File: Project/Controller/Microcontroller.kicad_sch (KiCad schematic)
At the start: 35 parts, among them J2 SWD Connector, J3 USB_B_Micro, SW1 SW_SPDT, SW2 SW_SPDT, SW3 SW_Push, U1 STM32F446RCTx, U2 TVS0500DRV, Y1 25 MHz

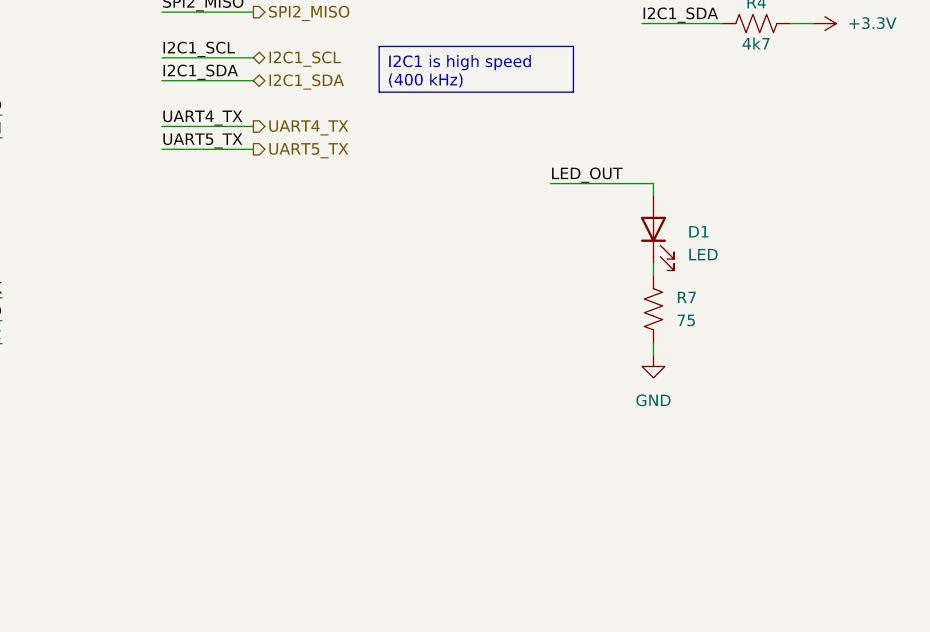
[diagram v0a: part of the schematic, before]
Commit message: Add 64 kb EEPROM
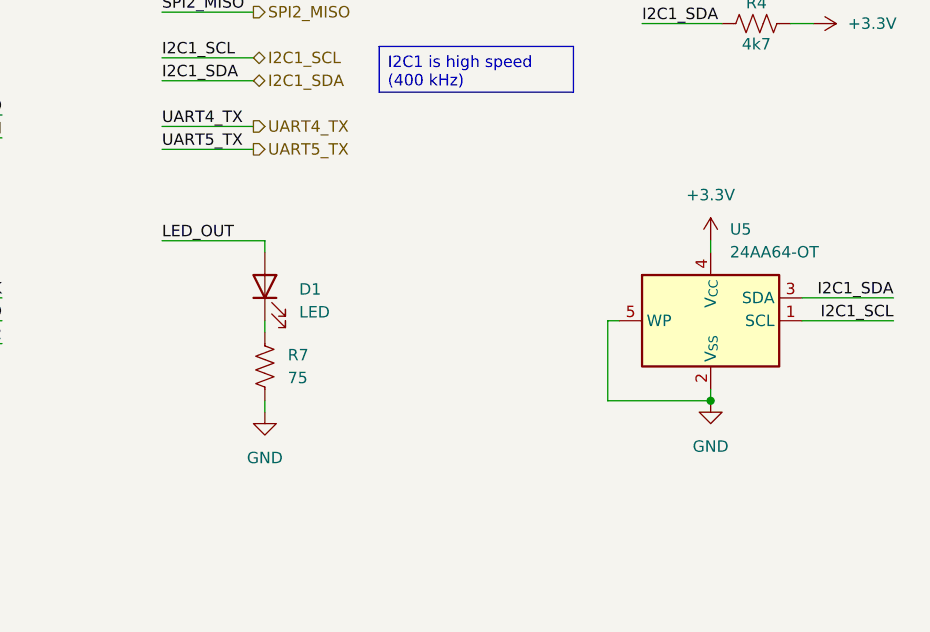
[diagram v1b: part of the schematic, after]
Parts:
- added U5: 24AA64-OT, Package_TO_SOT_SMD:SOT-23-5, symbol Memory_EEPROM:24AA02-OT
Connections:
- net +3.3V: now also U5.4 (V_{CC})
- net GND: now also U5.2 (V_{SS}), U5.5 (WP)
- net I2C1_SCL: now also U5.1 (SCL)
- net I2C1_SDA: now also U5.3 (SDA)
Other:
- moved on the sheet: D1, R7

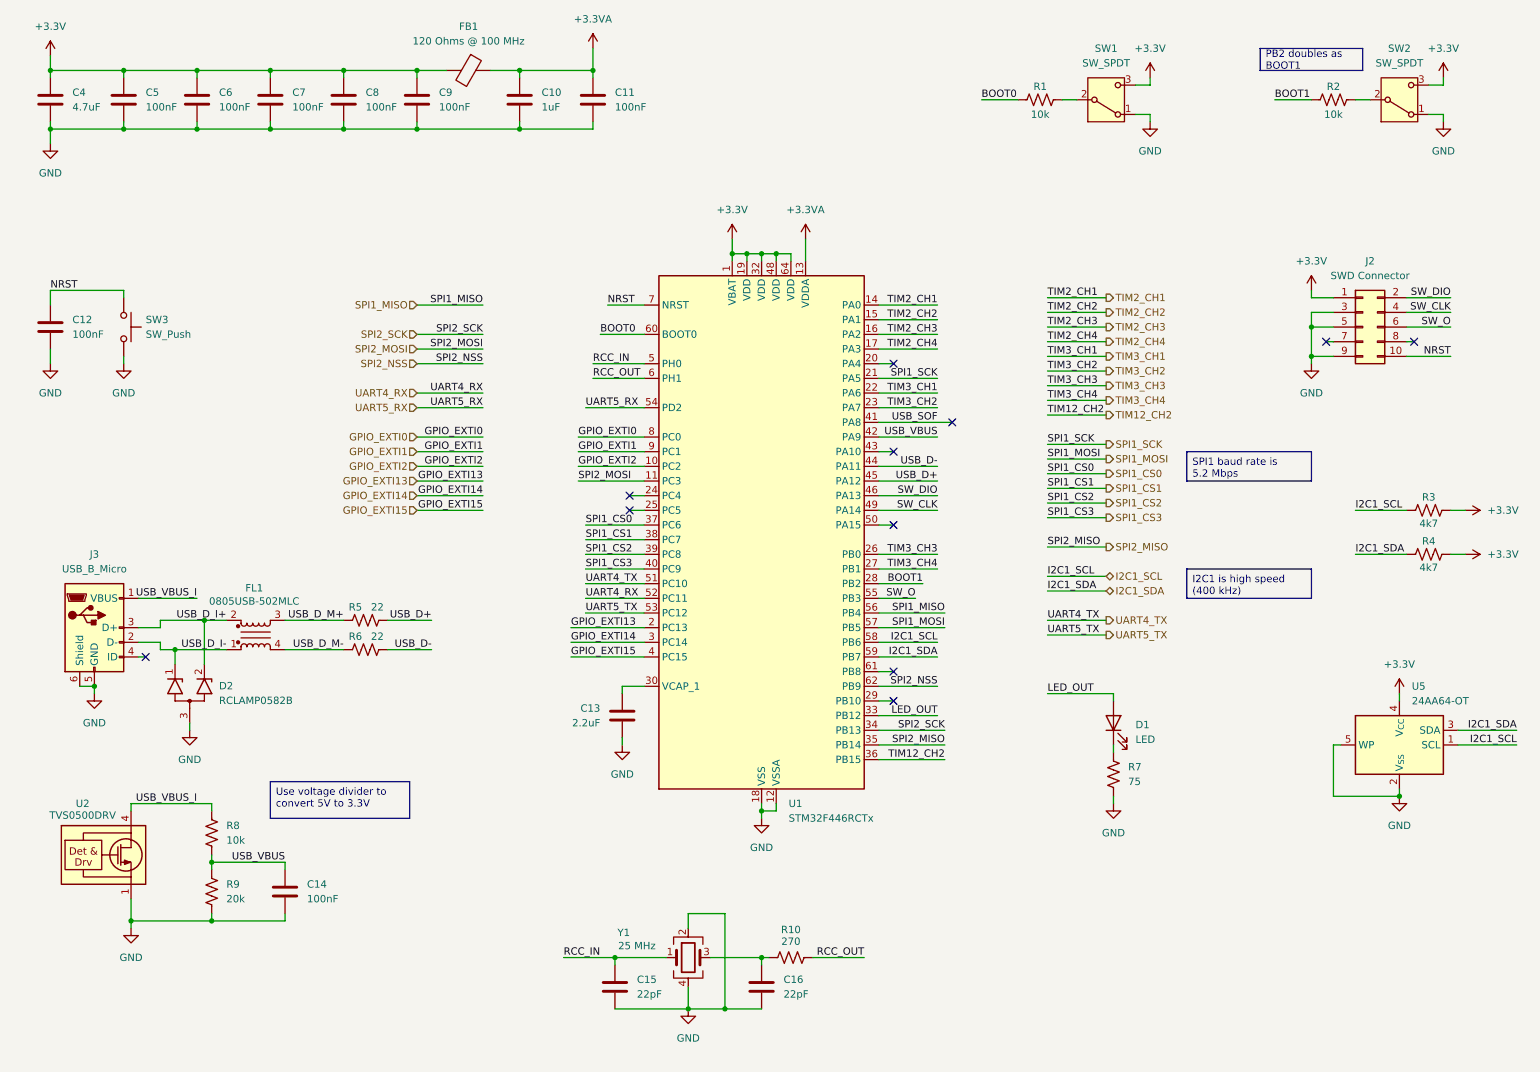
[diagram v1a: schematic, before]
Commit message: Add LDO to power input for controller board
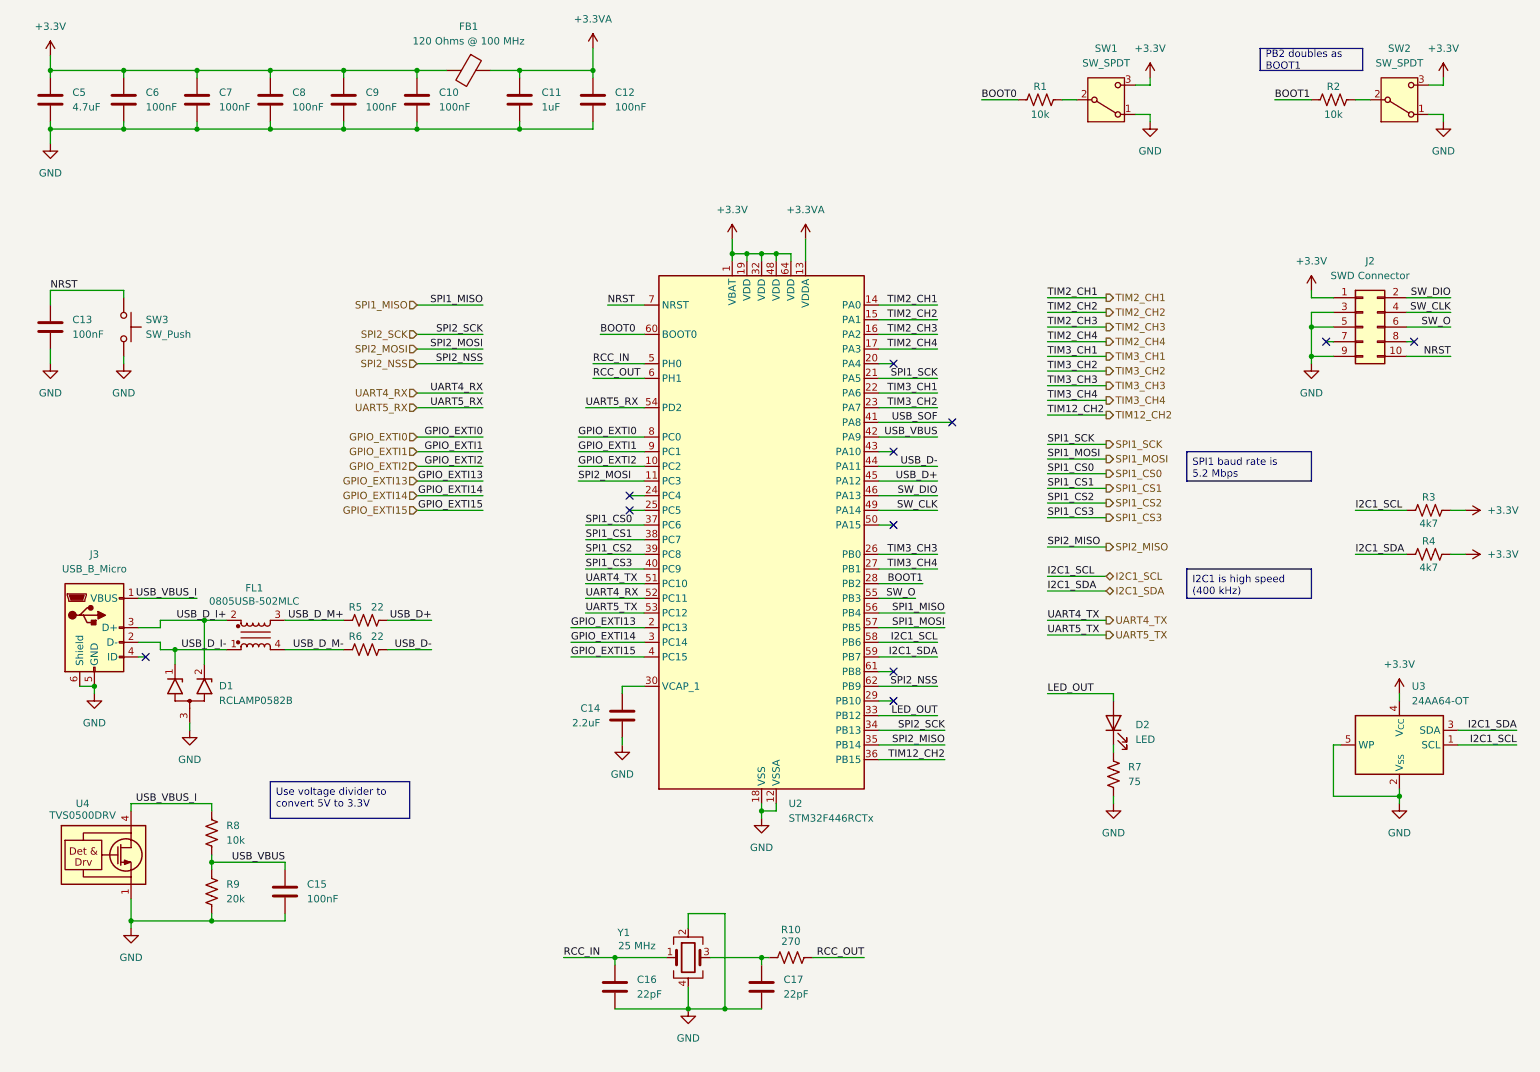
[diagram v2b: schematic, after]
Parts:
- renumbered C9 to C10, C10 to C11, C11 to C12, C12 to C13, C13 to C14, C14 to C15, C15 to C16, C16 to C17, C4 to C5, C5 to C6, C6 to C7, C7 to C8, C8 to C9, D2 to D1, D1 to D2, U1 to U2, U5 to U3, U2 to U4

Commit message: Change USB connector from USB-B Micro to USB-C
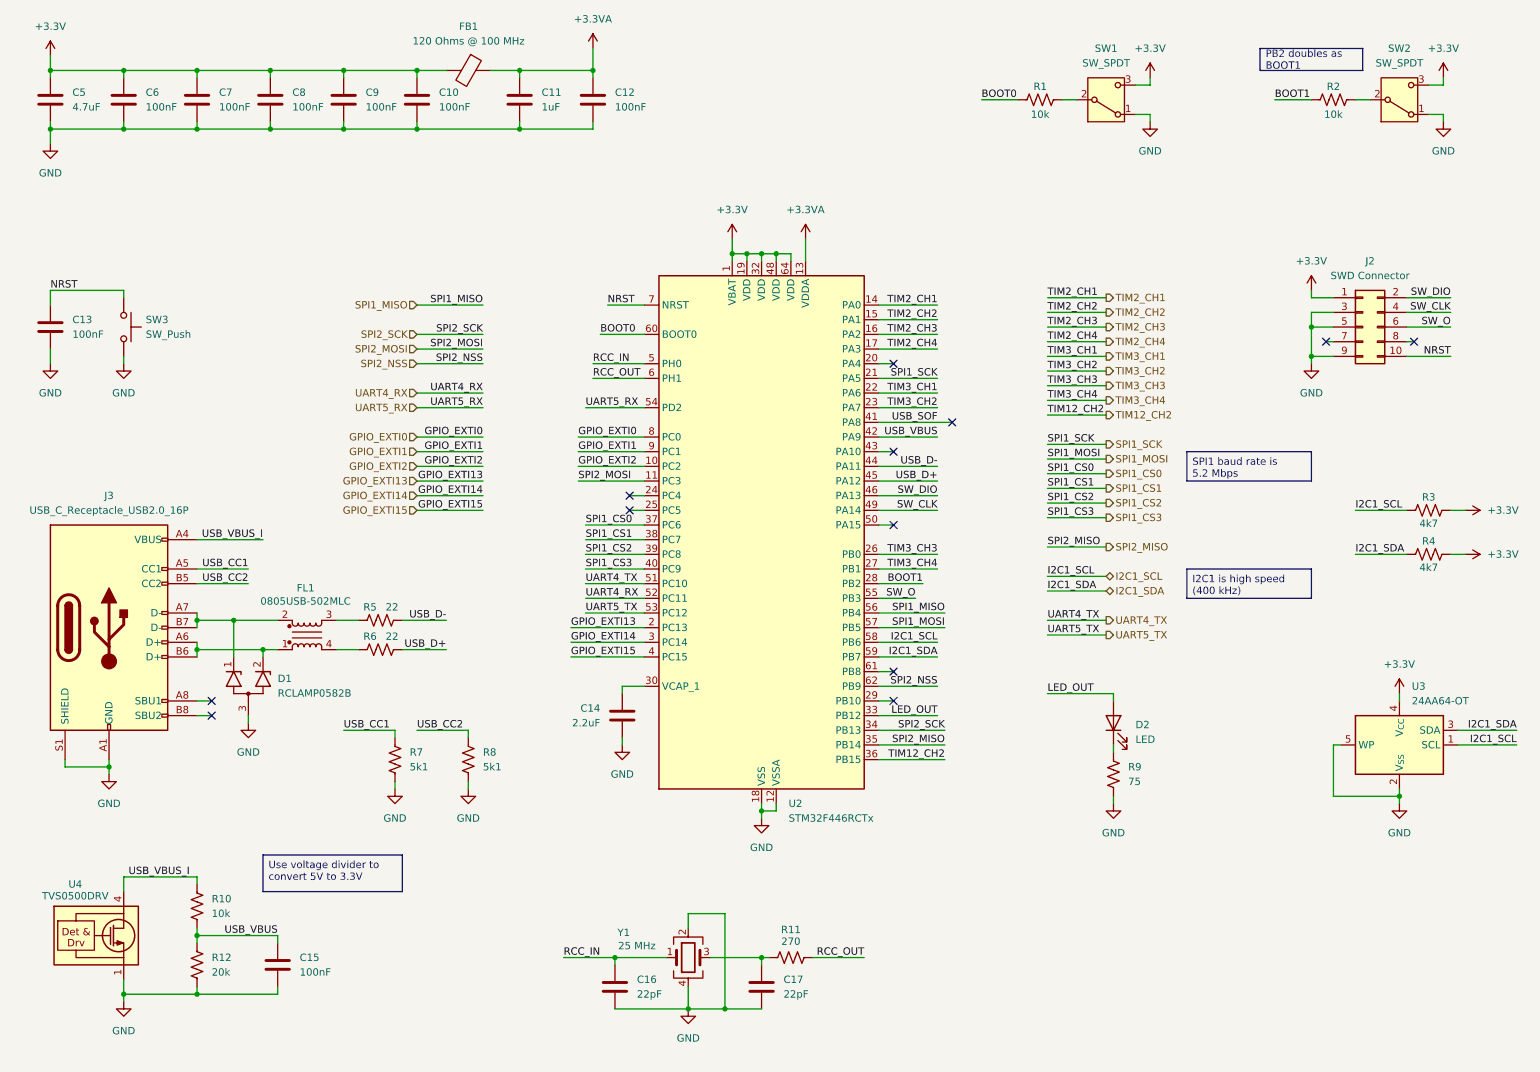
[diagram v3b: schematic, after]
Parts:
- removed J3: USB_B_Micro, Connector_USB:USB_Micro-B_Molex_47346-0001, symbol Connector:USB_B_Micro
- added J3: USB_C_Receptacle_USB2.0_16P, Connector_USB:USB_C_Receptacle_GCT_USB4105-xx-A_16P_TopMnt_Horizontal, symbol Connector:USB_C_Receptacle_USB2.0_16P
- added R7, R8: 5k1, Resistor_SMD:R_0603_1608Metric, symbol Device:R_US
- renumbered R8 to R10, R10 to R11, R9 to R12, R7 to R9
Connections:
- net GND: now also J3.A1 (GND), J3.A12 (GND), J3.B1 (GND), J3.B12 (GND), J3.S1 (SHIELD), R7.2, R8.2
- net USB_D+: now also R6.1; no longer R5.1
- net USB_D-: now also R5.1; no longer R6.1
- net USB_VBUS_I: now also J3.A4 (VBUS), J3.A9 (VBUS), J3.B4 (VBUS), J3.B9 (VBUS)
- net USB_D_I+: no longer names the net of D1.2 (K2)
- net USB_D_I+: now also FL1.1, J3.A6 (D+), J3.B6 (D+); no longer FL1.2
- net USB_D_I-: no longer names the net of D1.1 (K1)
- net USB_D_I-: now also FL1.2, J3.A7 (D-), J3.B7 (D-); no longer FL1.1
- net USB_D_M+: no longer names the net of FL1.3, R5.2
- net USB_D_M-: no longer names the net of FL1.4, R6.2
- new net USB_CC1: J3.A5 (CC1), R7.1
- new net USB_CC2: J3.B5 (CC2), R8.1
- no-connect marks 11 -> 12
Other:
- moved on the sheet: C15, D1, FL1, R10, R12, R5, R6, U4

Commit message: Change USB ESD chip to USBLC6
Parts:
- removed D1: RCLAMP0582B, Package_TO_SOT_SMD:SOT-416, symbol Power_Protection:RCLAMP0582B
- removed U4: TVS0500DRV, Package_SON:WSON-6-1EP_2x2mm_P0.65mm_EP1x1.6mm, symbol Power_Protection:TVS0500DRV
- added U3: USBLC6-2SC6, Package_TO_SOT_SMD:SOT-23-6, symbol Power_Protection:USBLC6-2SC6
- renumbered D2 to D1, U3 to U4
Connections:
- net GND: now also U3.2 (GND)
- net USB_VBUS_I: now also U3.5 (VBUS)
- net at J3.A6 (D+), J3.B6 (D+): now also U3.3 (I/O2); no longer FL1.1
- net at J3.A7 (D-), J3.B7 (D-): now also U3.1 (I/O1); no longer FL1.2
- net at R6.2: now also FL1.3; no longer FL1.4
- net at R5.2: now also FL1.4; no longer FL1.3
- new net: FL1.1, U3.6 (I/O1)
- new net: FL1.2, U3.4 (I/O2)
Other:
- moved on the sheet: C15, FL1, R10, R12, R5, R6, R7, R8

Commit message: Add ideal diode ORing for power connector and USB power
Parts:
- renumbered C8 to C10, C9 to C11, C10 to C12, C11 to C13, C12 to C14, C13 to C15, C14 to C16, C15 to C17, C16 to C18, C17 to C19, C5 to C7, C6 to C8, C7 to C9, D1 to D3, R7 to R10, R8 to R11, R9 to R12, R10 to R13, R11 to R14, R12 to R15, R1 to R4, R2 to R5, R3 to R6, R4 to R7, R5 to R8, R6 to R9, U2 to U4, U3 to U5, U4 to U6
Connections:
- net USB_VBUS_I renamed USB_Power

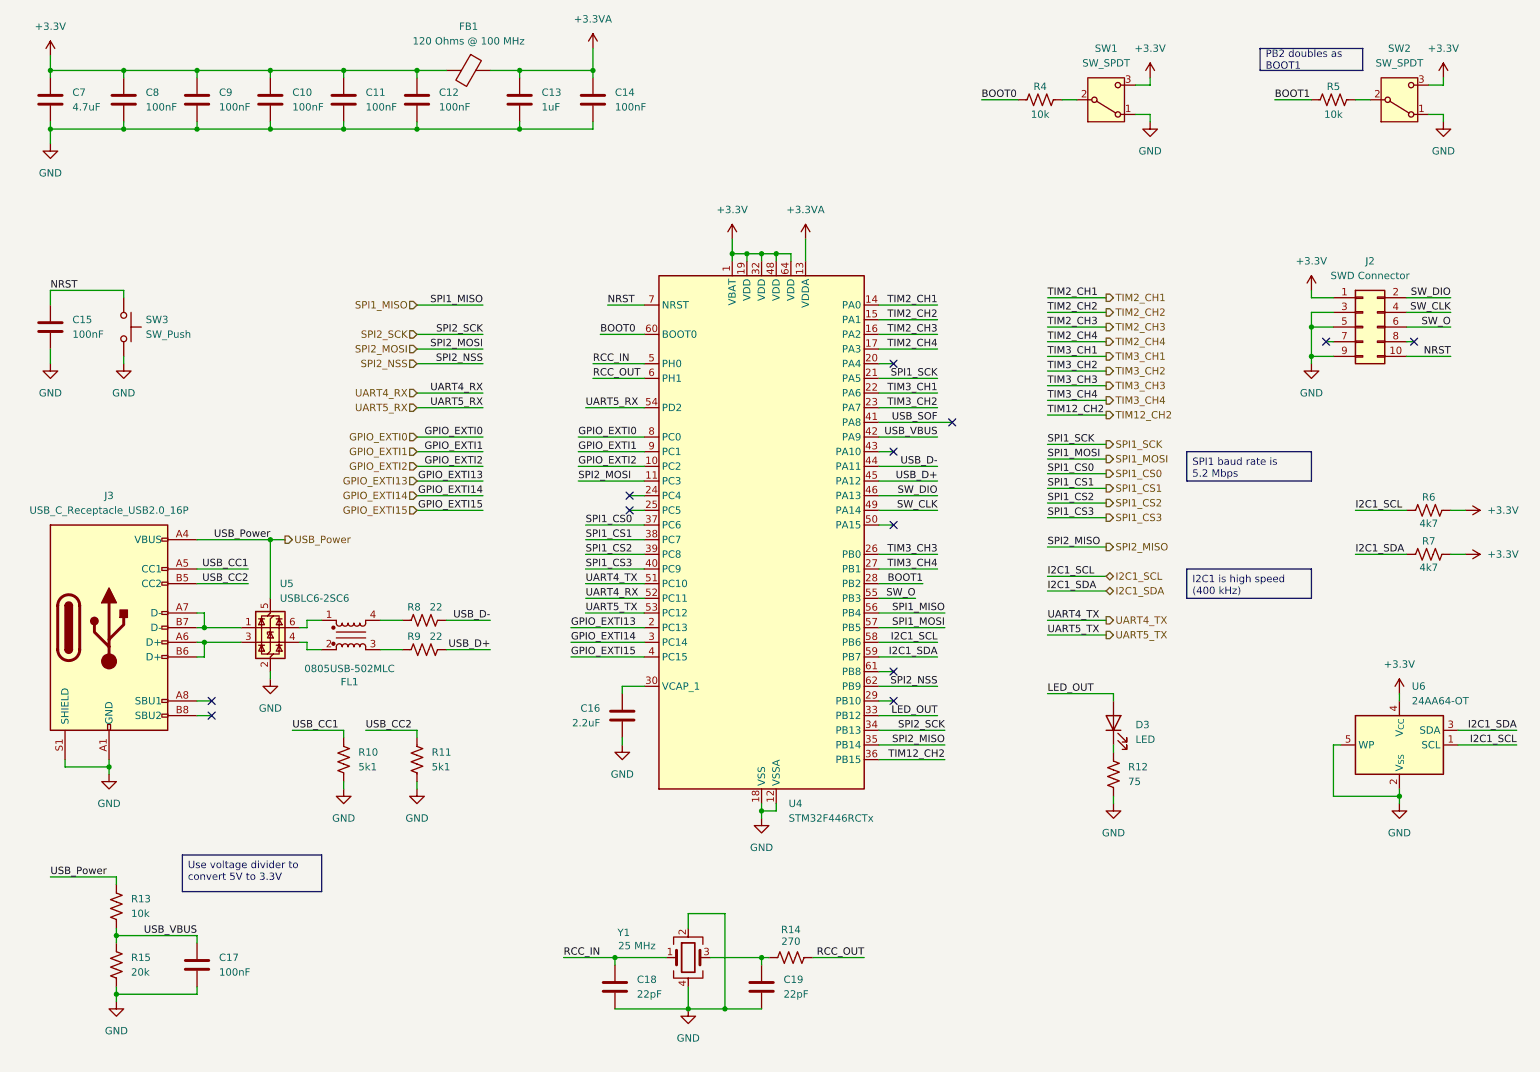
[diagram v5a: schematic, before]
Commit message: Reorganize microcontroller schematic
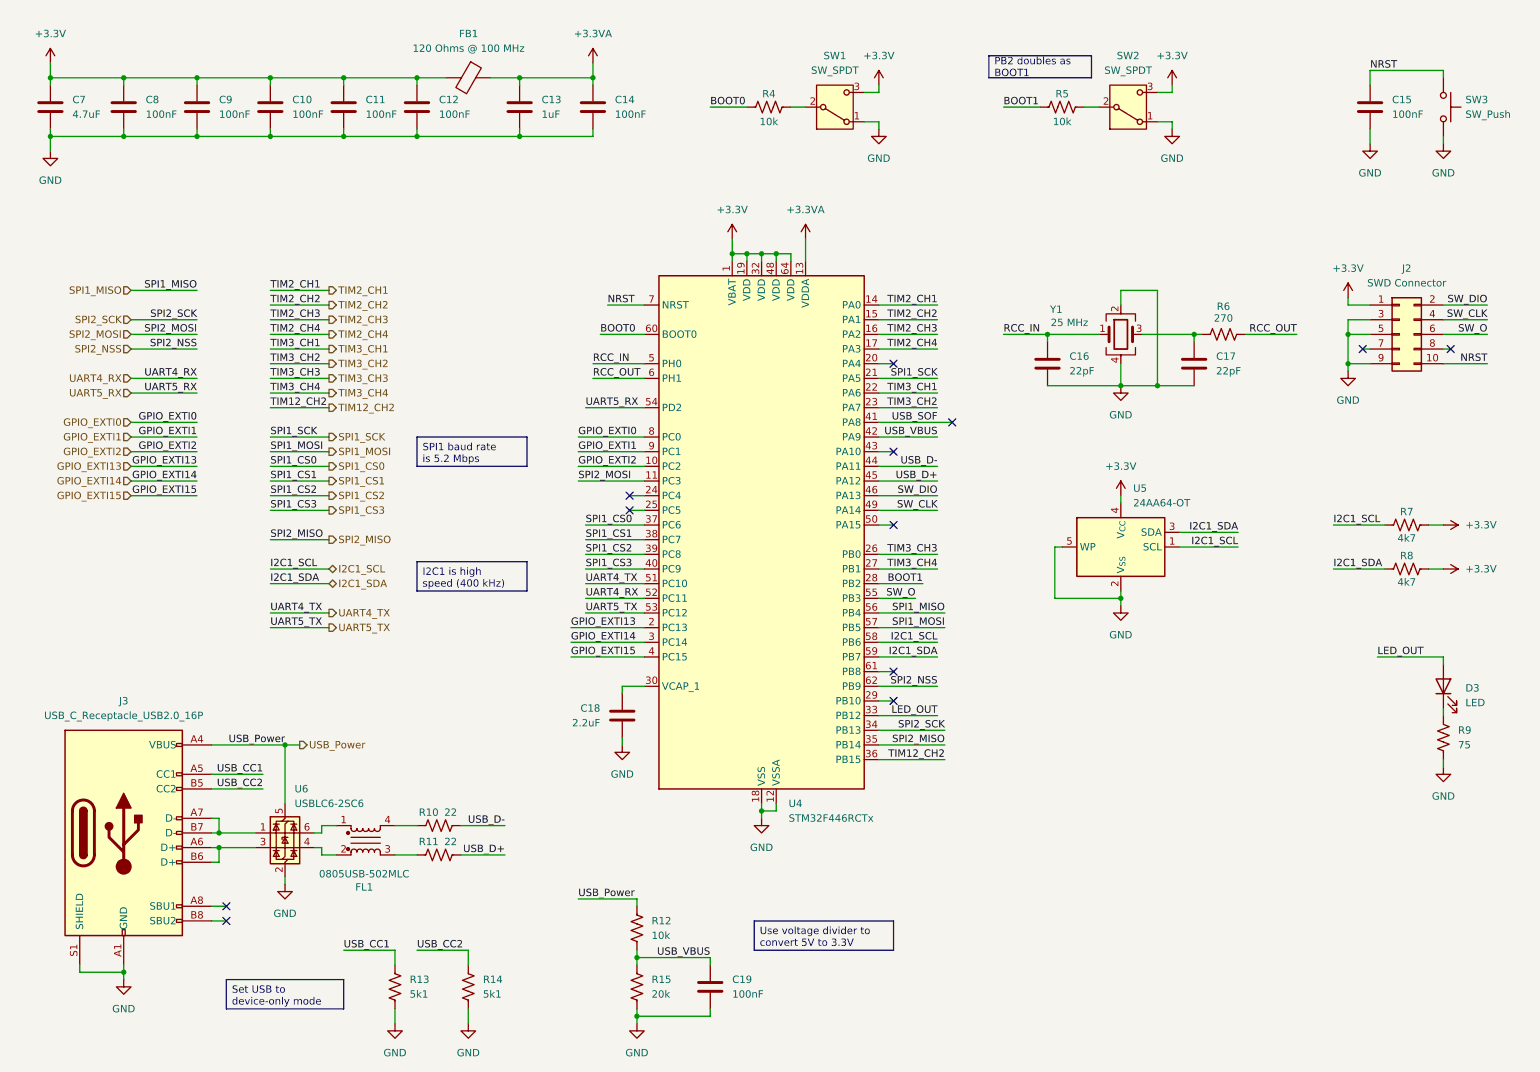
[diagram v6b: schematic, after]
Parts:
- renumbered C18 to C16, C19 to C17, C16 to C18, C17 to C19, R8 to R10, R9 to R11, R13 to R12, R10 to R13, R11 to R14, R14 to R6, R6 to R7, R7 to R8, R12 to R9, U6 to U5, U5 to U6
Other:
- moved on the sheet: C10, C11, C12, C13, C14, C15, C16, C17, C19, C7, C8, C9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
